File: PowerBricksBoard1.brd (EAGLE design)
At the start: 76.2 x 50.8 mm, 13 parts

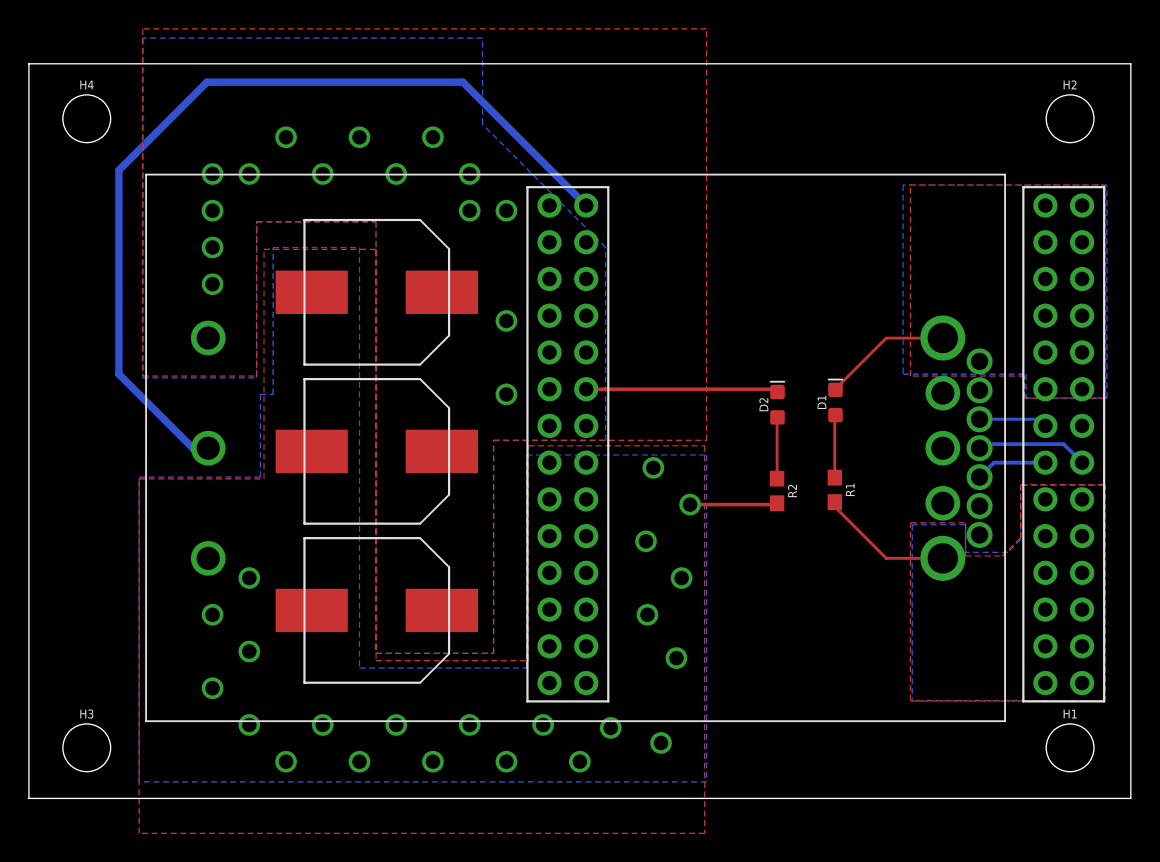
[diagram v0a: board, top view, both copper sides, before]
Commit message: cad for connectors
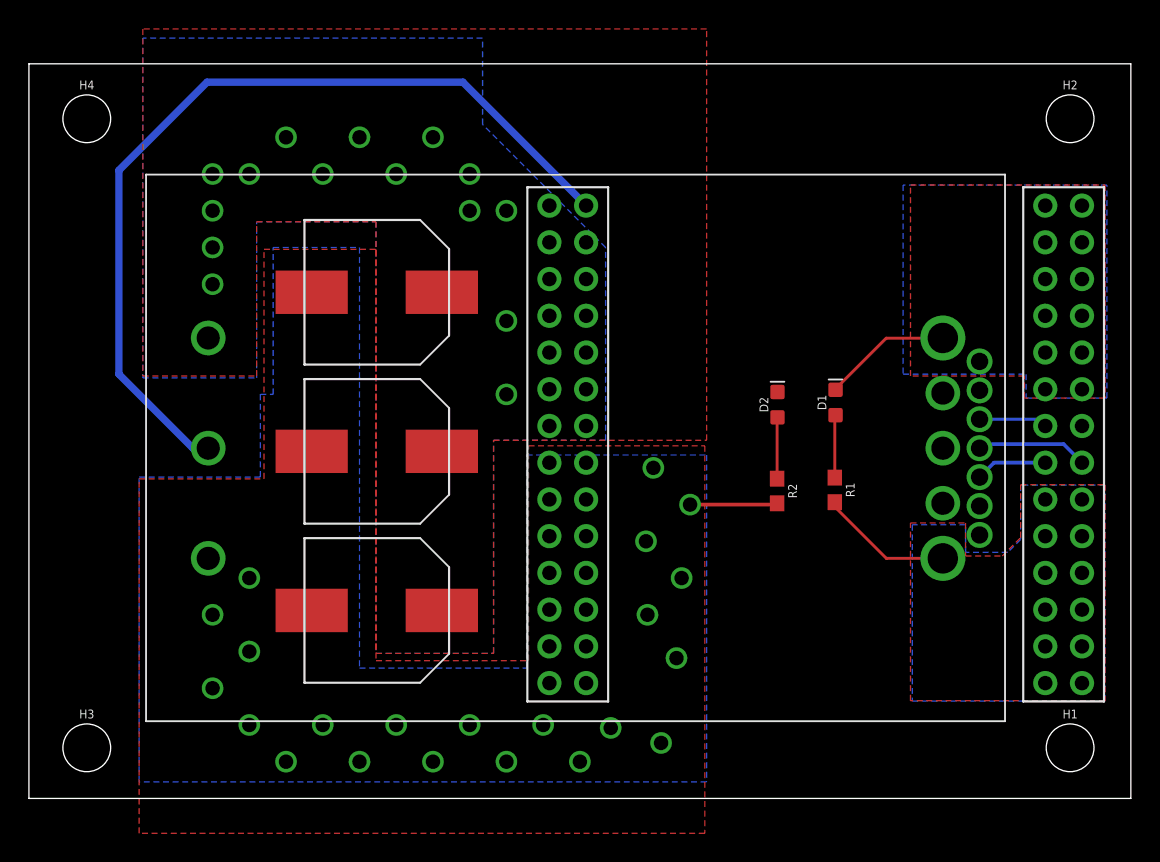
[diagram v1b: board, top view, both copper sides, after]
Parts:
- removed U$5: BRICKBOARD_TSW_14X2, Dist_to_Brickboard_Connector:BRICKBOARD_TSW_14X2
- added U$6: BRICKBOARD_TSW_14X2, Dist_to_Brickboard_Connector_brick:BRICKBOARD_TSW_14X2
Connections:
- net 12V: now also U$6.45, U$6.46, U$6.47, U$6.48, U$6.49, U$6.50, U$6.51, U$6.52, U$6.53, U$6.54, U$6.55, U$6.56; no longer U$5.45, U$5.46, U$5.47, U$5.48, U$5.49, U$5.50, U$5.51, U$5.52, U$5.53, U$5.54, U$5.55, U$5.56
- net 12_GND: now also U$6.29, U$6.30, U$6.31, U$6.32, U$6.33, U$6.34, U$6.35, U$6.36, U$6.37, U$6.38, U$6.39, U$6.40; no longer U$5.29, U$5.30, U$5.31, U$5.32, U$5.33, U$5.34, U$5.35, U$5.36, U$5.37, U$5.38, U$5.39, U$5.40
- net 48V: now also U$6.15, U$6.16, U$6.17, U$6.18, U$6.19, U$6.20, U$6.21, U$6.22, U$6.23, U$6.24, U$6.25, U$6.26, U$6.27, U$6.28; no longer U$5.15, U$5.16, U$5.17, U$5.18, U$5.19, U$5.20, U$5.21, U$5.22, U$5.23, U$5.24, U$5.25, U$5.26, U$5.27, U$5.28
- net 48_GND: now also U$6.10, U$6.11, U$6.12, U$6.13, U$6.14, U$6.3, U$6.4, U$6.5, U$6.6, U$6.7, U$6.8, U$6.9; no longer U$5.10, U$5.11, U$5.12, U$5.13, U$5.14, U$5.3, U$5.4, U$5.5, U$5.6, U$5.7, U$5.8, U$5.9
- net ALERT: now also U$6.43; no longer U$5.43
- net CLK: now also U$6.44; no longer U$5.44
- net DATA: now also U$6.42; no longer U$5.42
- net ON/OFF: now also U$6.1; no longer U$5.1
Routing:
- net 48_GND: track 13.3 -> 0.27 mm

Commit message: Filled caps & ADDR resistors
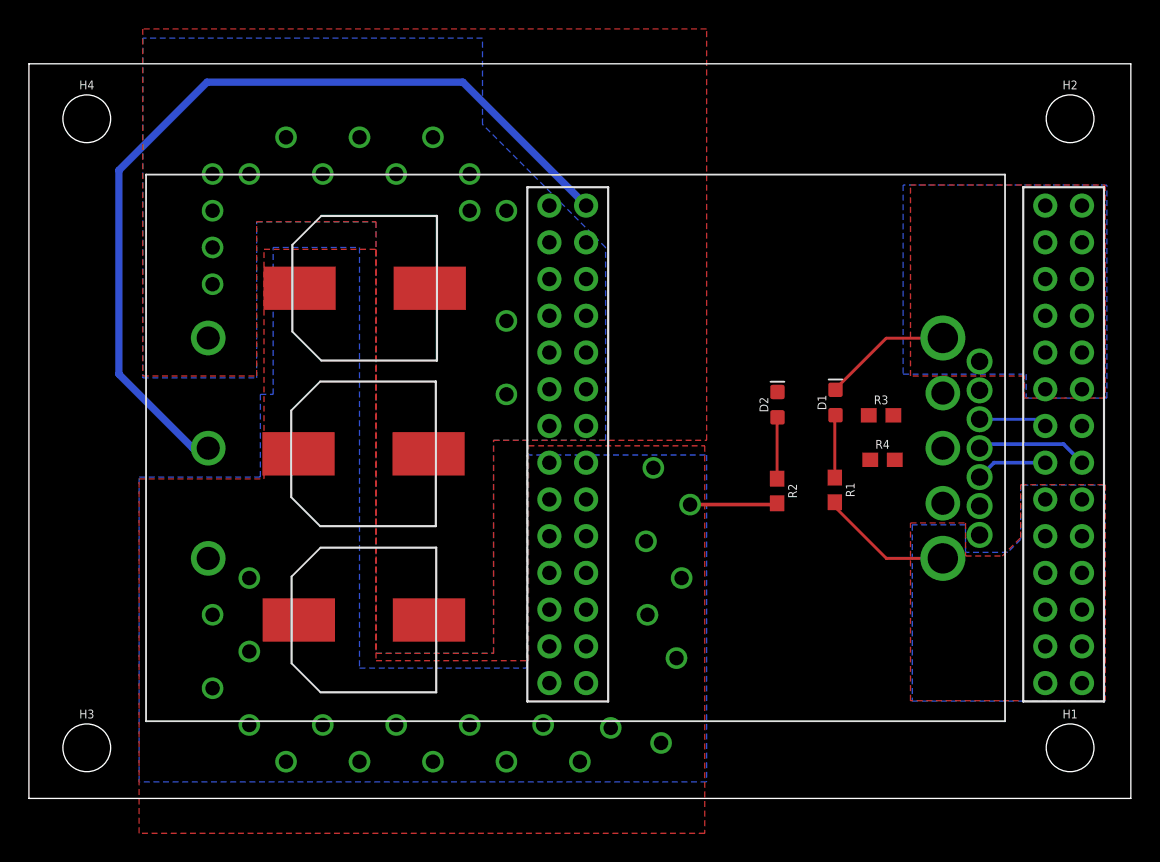
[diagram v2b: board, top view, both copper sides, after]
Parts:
- added R3, R4: (no value), SparkFun-Resistors:0603
- moved U$4 1.11 mm to (23.2, 12.3), turned to 90 degrees
- moved U$2 0.93 mm to (23.1, 23.8), turned to 90 degrees
- moved U$3 0.88 mm to (23.2, 35.3), turned to 90 degrees
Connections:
- new net DGND: R3.1, R4.1, U$1.DGND
- new net N$3: R3.2, U$1.ADDR1
- new net N$4: R4.2, U$1.ADDR0
- net 48V: now also U$2.P$2, U$3.P$2, U$4.P$2; no longer U$2.P$1, U$3.P$1, U$4.P$1
- net 48_GND: now also U$2.P$1, U$3.P$1, U$4.P$1; no longer U$2.P$2, U$3.P$2, U$4.P$2
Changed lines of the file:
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@@
 <?xml version="1.0" encoding="utf-8"?>
 <!DOCTYPE eagle SYSTEM "eagle.dtd">
-<eagle version="9.6.2">
+<eagle version="9.5.0">
 <drawing>
 <settings>
@@
 </autorouter>
 <elements>
-<element name="U$2" library="UCM1H331MNL1GS" package="UCM1H331MNL1GS" value="UCM1H331MNL1GS" x="24.0538" y="24" smashed="yes" rot="R270"/>
-<element name="U$3" library="UCM1H331MNL1GS" package="UCM1H331MNL1GS" value="UCM1H331MNL1GS" x="24.0538" y="35.0012" smashed="yes" rot="R270"/>
-<element name="U$4" library="UCM1H331MNL1GS" package="UCM1H331MNL1GS" value="UCM1H331MNL1GS" x="24.0538" y="13" smashed="yes" rot="R270"/>
+<element name="U$2" library="UCM1H331MNL1GS" package="UCM1H331MNL1GS" value="UCM1H331MNL1GS" x="23.1394" y="23.8282" smashed="yes" rot="R90"/>
+<element name="U$3" library="UCM1H331MNL1GS" package="UCM1H331MNL1GS" value="UCM1H331MNL1GS" x="23.2156" y="35.2806" smashed="yes" rot="R90"/>
+<element name="U$4" library="UCM1H331MNL1GS" package="UCM1H331MNL1GS" value="UCM1H331MNL1GS" x="23.1648" y="12.3396" smashed="yes" rot="R90"/>
 <element name="H1" library="SparkFun-Hardware" library_urn="urn:adsk.eagle:library:519" package="STAND-OFF" package3d_urn="urn:adsk.eagle:package:38630/1" value="STAND-OFF" x="72" y="3.5" smashed="yes">
 <attribute name="NAME" x="72" y="5.532" size="0.6096" layer="25" font="vector" ratio="20" align="bottom-center"/>
@@
 </element>
 <element name="U$6" library="Dist_to_Brickboard_Connector_brick" package="BRICKBOARD_TSW_14X2" package3d_urn="urn:adsk.eagle:package:23225958/2" value="BRICKBOARD_TSW_14X2" x="35.9918" y="40.9956" smashed="yes" rot="R270"/>
+<element name="R3" library="SparkFun-Resistors" library_urn="urn:adsk.eagle:library:532" package="0603" package3d_urn="urn:adsk.eagle:package:39650/1" value=" " x="58.928" y="26.4922" smashed="yes">
+<attribute name="NAME" x="58.928" y="27.2542" size="0.6096" layer="25" font="vector" ratio="20" align="bottom-center"/>
+<attribute name="PROD_ID" value=" " x="58.928" y="26.4922" size="1.778" layer="27" display="off"/>
+<attribute name="VALUE" x="58.928" y="25.7302" size="0.6096" layer="27" font="vector" ratio="20" align="top-center"/>
+</element>
+<element name="R4" library="SparkFun-Resistors" library_urn="urn:adsk.eagle:library:532" package="0603" package3d_urn="urn:adsk.eagle:package:39650/1" value=" " x="59.0296" y="23.4188" smashed="yes">
+<attribute name="NAME" x="59.0296" y="24.1808" size="0.6096" layer="25" font="vector" ratio="20" align="bottom-center"/>
+<attribute name="PROD_ID" value=" " x="59.0296" y="23.4188" size="1.778" layer="27" display="off"/>
+<attribute name="VALUE" x="59.0296" y="22.6568" size="0.6096" layer="27" font="vector" ratio="20" align="top-center"/>
+</element>
 </elements>
 <signals>
 <signal name="48V">
-<contactref element="U$2" pad="P$1"/>
-<contactref element="U$3" pad="P$1"/>
-<contactref element="U$4" pad="P$1"/>
 <contactref element="U$1" pad="48V"/>
 <polygon width="0.508" layer="1" isolate="0.762" thermals="no" rank="2">
@@
 <contactref element="U$6" pad="25"/>
 <contactref element="U$6" pad="27"/>
+<contactref element="U$2" pad="P$2"/>
+<contactref element="U$3" pad="P$2"/>
+<contactref element="U$4" pad="P$2"/>
 </signal>
 <signal name="48_GND">
-<contactref element="U$4" pad="P$2"/>
-<contactref element="U$3" pad="P$2"/>
-<contactref element="U$2" pad="P$2"/>
 <contactref element="U$1" pad="48V_GND"/>
 <polygon width="0.508" layer="1" isolate="0.762" thermals="no">
@@
 <contactref element="U$6" pad="11"/>
 <contactref element="U$6" pad="13"/>
+<contactref element="U$2" pad="P$1"/>
+<contactref element="U$3" pad="P$1"/>
+<contactref element="U$4" pad="P$1"/>
 <wire x1="38.5318" y1="28.2956" x2="51.571" y2="28.3" width="0" layer="19" extent="1-1"/>
 </signal>
@@
 <wire x1="51.7652" y1="26.3518" x2="51.7398" y2="26.3264" width="0.2032" layer="1"/>
 </signal>
+<signal name="DGND">
+<contactref element="U$1" pad="DGND"/>
+<contactref element="R3" pad="1"/>
+<contactref element="R4" pad="1"/>
+<wire x1="58.078" y1="26.4922" x2="65.74" y2="28.22" width="0" layer="19" extent="1-1"/>
+<wire x1="58.1796" y1="23.4188" x2="58.078" y2="26.4922" width="0" layer="19" extent="1-1"/>
+</signal>
+<signal name="N$3">
+<contactref element="U$1" pad="ADDR1"/>
+<contactref element="R3" pad="2"/>
+<wire x1="65.74" y1="20.22" x2="59.778" y2="26.4922" width="0" layer="19" extent="1-1"/>
+</signal>
+<signal name="N$4">
+<contactref element="U$1" pad="ADDR0"/>
+<contactref element="R4" pad="2"/>
+<wire x1="59.8796" y1="23.4188" x2="65.74" y2="18.22" width="0" layer="19" extent="1-1"/>
+</signal>
 </signals>
